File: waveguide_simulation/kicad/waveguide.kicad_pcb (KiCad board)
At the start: 2 copper layers, 5 x 5 mm, 0 parts

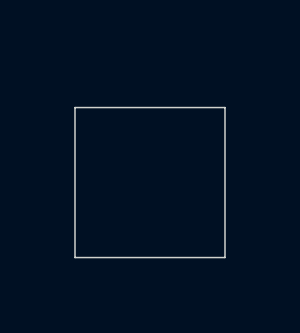
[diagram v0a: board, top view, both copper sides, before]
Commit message: [waveguide_simulation] Attempt at simulation failed, see files in relevant folder | TODO: check non-macro example (purely pcb import macro not openems macro) or check working examples first
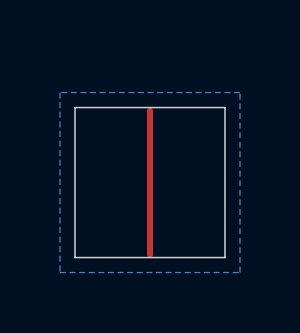
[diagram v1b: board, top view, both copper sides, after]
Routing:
- net (no net): track 0.00 -> 4.80 mm
- added copper zone on B.Cu, net (none)
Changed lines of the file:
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@@
 		(layer "Edge.Cuts")
 	)
+	(segment
+		(start 102.5 52.5)
+		(end 102.5 54.9)
+		(width 0.2)
+		(layer "F.Cu")
+		(net 0)
+	)
+	(segment
+		(start 102.5 50.1)
+		(end 102.5 52.5)
+		(width 0.2)
+		(layer "F.Cu")
+		(net 0)
+	)
+	(zone
+		(net 0)
+		(net_name "")
+		(layer "B.Cu")
+		(hatch edge 0.5)
+		(connect_pads
+			(clearance 0.5)
+		)
+		(min_thickness 0.25)
+		(filled_areas_thickness no)
+		(fill yes
+			(thermal_gap 0.5)
+			(thermal_bridge_width 0.5)
+			(island_removal_mode 1)
+			(island_area_min 10)
+		)
+		(polygon
+			(pts
+				(xy 99.5 49.5) (xy 99.5 55.5) (xy 105.5 55.5) (xy 105.5 49.5)
+			)
+		)
+	)
 )

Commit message: update waveguide and kicad project
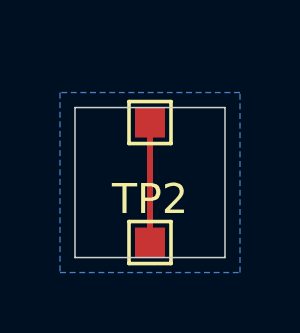
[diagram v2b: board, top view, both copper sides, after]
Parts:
- added TP1: TestPoint, TestPoint:TestPoint_Pad_1.0x1.0mm, F.Cu at (102.5, 50.5)
- added TP2: TestPoint, TestPoint:TestPoint_Pad_1.0x1.0mm, F.Cu at (102.5, 54.5)
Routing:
- net test: track 0.00 -> 4.80 mm
- net (no net): track 4.80 -> 0.00 mm

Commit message: experimented with meshing on planar waveguide
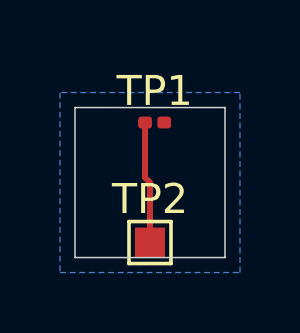
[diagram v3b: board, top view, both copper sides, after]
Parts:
- TP1: footprint TestPoint:TestPoint_Pad_1.0x1.0mm -> Resistor_SMD:R_0201_0603Metric
- moved TP1 0.16 mm to (102.7, 50.5)
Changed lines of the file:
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@@
 	(net 0 "")
 	(net 1 "test")
+	(footprint "Resistor_SMD:R_0201_0603Metric"
+		(layer "F.Cu")
+		(at 102.655 50.5)
+		(descr "Resistor SMD 0201 (0603 Metric), square (rectangular) end terminal, IPC_7351 nominal, (Body size source: https://www.vishay.com/docs/20052/crcw0201e3.pdf), generated with kicad-footprint-generator")
+		(tags "resistor")
+		(property "Reference" "TP1"
+			(at 0 -1.05 0)
+			(layer "F.SilkS")
+			(effects
+				(font
+					(size 1 1)
+					(thickness 0.15)
+				)
+			)
+		)
+		(property "Value" "TestPoint"
+			(at 0 1.05 0)
+			(layer "F.Fab")
+			(hide yes)
+			(effects
+				(font
+					(size 1 1)
+					(thickness 0.15)
+				)
+			)
+		)
+		(property "Footprint" "Resistor_SMD:R_0201_0603Metric"
+			(at 0 0 0)
+			(unlocked yes)
+			(layer "F.Fab")
+			(hide yes)
+			(effects
+				(font
+					(size 1.27 1.27)
+					(thickness 0.15)
+				)
+			)
+		)
+		(property "Datasheet" ""
+			(at 0 0 0)
+			(unlocked yes)
+			(layer "F.Fab")
+			(hide yes)
+			(effects
+				(font
+					(size 1.27 1.27)
+					(thickness 0.15)
+				)
+			)
+		)
+		(property "Description" "test point"
+			(at 0 0 0)
+			(unlocked yes)
+			(layer "F.Fab")
+			(hide yes)
+			(effects
+				(font
+					(size 1.27 1.27)
+					(thickness 0.15)
+				)
+			)
+		)
+		(property ki_fp_filters "Pin* Test*")
+		(sheetname "Root")
+		(sheetfile "waveguide.kicad_sch")
+		(attr smd)
+		(fp_line
+			(start -0.7 -0.35)
+			(end 0.7 -0.35)
+			(stroke
+				(width 0.05)
+				(type solid)
+			)
+			(layer "F.CrtYd")
+		)
+		(fp_line
+			(start -0.7 0.35)
+			(end -0.7 -0.35)
+			(stroke
+				(width 0.05)
+				(type solid)
+			)
+			(layer "F.CrtYd")
+		)
+		(fp_line
+			(start 0.7 -0.35)
+			(end 0.7 0.35)
+			(stroke
+				(width 0.05)
+				(type solid)
+			)
+			(layer "F.CrtYd")
+		)
+		(fp_line
+			(start 0.7 0.35)
+			(end -0.7 0.35)
+			(stroke
+				(width 0.05)
+				(type solid)
+			)
+			(layer "F.CrtYd")
+		)
+		(fp_line
+			(start -0.3 -0.15)
+			(end 0.3 -0.15)
+			(stroke
+				(width 0.1)
+				(type solid)
+			)
+			(layer "F.Fab")
+		)
+		(fp_line
+			(start -0.3 0.15)
+			(end -0.3 -0.15)
+			(stroke
+				(width 0.1)
+				(type solid)
+			)
+			(layer "F.Fab")
+		)
+		(fp_line
+			(start 0.3 -0.15)
+			(end 0.3 0.15)
+			(stroke
+				(width 0.1)
+				(type solid)
+			)
+			(layer "F.Fab")
+		)
+		(fp_line
+			(start 0.3 0.15)
+			(end -0.3 0.15)
+			(stroke
+				(width 0.1)
+				(type solid)
+			)
+			(layer "F.Fab")
+		)
+		(fp_text user "${REFERENCE}"
+			(at 0 -0.68 0)
+			(layer "F.Fab")
+			(effects
+				(font
+					(size 0.25 0.25)
+					(thickness 0.04)
+				)
+			)
+		)
+		(pad "" smd roundrect
+			(at -0.345 0)
+			(size 0.318 0.36)
+			(layers "F.Paste")
+			(roundrect_rratio 0.25)
+		)
+		(pad "" smd roundrect
+			(at 0.345 0)
+			(size 0.318 0.36)
+			(layers "F.Paste")
+			(roundrect_rratio 0.25)
+		)
+		(pad "1" smd roundrect
+			(at -0.32 0)
+			(size 0.46 0.4)
+			(layers "F.Cu" "F.Mask")
+			(roundrect_rratio 0.25)
+			(net 1 "test")
+			(pinfunction "1")
+			(pintype "passive")
+		)
+		(pad "2" smd roundrect
+			(at 0.32 0)
+			(size 0.46 0.4)
+			(layers "F.Cu" "F.Mask")
+			(roundrect_rratio 0.25)
+		)
+		(model "${KICAD8_3DMODEL_DIR}/Resistor_SMD.3dshapes/R_0201_0603Metric.wrl"
+			(offset
+				(xyz 0 0 0)
+			)
+			(scale
+				(xyz 1 1 1)
+			)
+			(rotate
+				(xyz 0 0 0)
+			)
+		)
+	)
 	(footprint "TestPoint:TestPoint_Pad_1.0x1.0mm"
 		(layer "F.Cu")
-		(at 102.5 50.5)
+		(at 102.5 54.5)
 		(descr "SMD rectangular pad as test Point, square 1.0mm side length")
 		(tags "test point SMD pad rectangle square")
-		(property "Reference" "TP1"
+		(property "Reference" "TP2"
 			(at 0 -1.448 0)
 			(layer "F.SilkS")
-			(hide yes)
 			(effects
 				(font
@@
 			)
 			(layer "F.CrtYd")
+		)
+		(fp_text user "${REFERENCE}"
+			(at 0 -1.45 0)
+			(layer "F.Fab")
+			(effects
+				(font
+					(size 1 1)
+					(thickness 0.15)
+				)
+			)
 		)
 		(pad "1" smd rect
@@
 		)
 	)
-	(footprint "TestPoint:TestPoint_Pad_1.0x1.0mm"
-		(layer "F.Cu")
-		(at 102.5 54.5)
-		(descr "SMD rectangular pad as test Point, square 1.0mm side length")
-		(tags "test point SMD pad rectangle square")
-		(property "Reference" "TP2"
-			(at 0 -1.448 0)
-			(layer "F.SilkS")
-			(effects
-				(font
-					(size 1 1)
-					(thickness 0.15)
-				)
-			)
-		)
-		(property "Value" "TestPoint"
-			(at 0 1.55 0)
-			(layer "F.Fab")
-			(effects
-				(font
-					(size 1 1)
-					(thickness 0.15)
-				)
-			)
-		)
-		(property "Footprint" "TestPoint:TestPoint_Pad_1.0x1.0mm"
-			(at 0 0 0)
-			(unlocked yes)
-			(layer "F.Fab")
-			(hide yes)
-			(effects
-				(font
-					(size 1.27 1.27)
-					(thickness 0.15)
-				)
-			)
-		)
-		(property "Datasheet" ""
-			(at 0 0 0)
-			(unlocked yes)
-			(layer "F.Fab")
-			(hide yes)
-			(effects
-				(font
-					(size 1.27 1.27)
-					(thickness 0.15)
-				)
-			)
-		)
-		(property "Description" "test point"
-			(at 0 0 0)
-			(unlocked yes)
-			(layer "F.Fab")
-			(hide yes)
-			(effects
-				(font
-					(size 1.27 1.27)
-					(thickness 0.15)
-				)
-			)
-		)
-		(property ki_fp_filters "Pin* Test*")
-		(sheetname "Root")
-		(sheetfile "waveguide.kicad_sch")
-		(attr exclude_from_pos_files)
-		(fp_line
-			(start -0.7 -0.7)
-			(end 0.7 -0.7)
-			(stroke
-				(width 0.12)
-				(type solid)
-			)
-			(layer "F.SilkS")
-		)
-		(fp_line
-			(start -0.7 0.7)
-			(end -0.7 -0.7)
-			(stroke
-				(width 0.12)
-				(type solid)
-			)
-			(layer "F.SilkS")
-		)
-		(fp_line
-			(start 0.7 -0.7)
-			(end 0.7 0.7)
-			(stroke
-				(width 0.12)
-				(type solid)
-			)
-			(layer "F.SilkS")
-		)
-		(fp_line
-			(start 0.7 0.7)
-			(end -0.7 0.7)
-			(stroke
-				(width 0.12)
-				(type solid)
-			)
-			(layer "F.SilkS")
-		)
-		(fp_line
-			(start -1 -1)
-			(end -1 1)
-			(stroke
-				(width 0.05)
-				(type solid)
-			)
-			(layer "F.CrtYd")
-		)
-		(fp_line
-			(start -1 -1)
-			(end 1 -1)
-			(stroke
-				(width 0.05)
-				(type solid)
-			)
-			(layer "F.CrtYd")
-		)
-		(fp_line
-			(start 1 1)
-			(end -1 1)
-			(stroke
-				(width 0.05)
-				(type solid)
-			)
-			(layer "F.CrtYd")
-		)
-		(fp_line
-			(start 1 1)
-			(end 1 -1)
-			(stroke
-				(width 0.05)
-				(type solid)
-			)
-			(layer "F.CrtYd")
-		)
-		(fp_text user "${REFERENCE}"
-			(at 0 -1.45 0)
-			(layer "F.Fab")
-			(effects
-				(font
-					(size 1 1)
-					(thickness 0.15)
-				)
-			)
-		)
-		(pad "1" smd rect
-			(at 0 0)
-			(size 1 1)
-			(layers "F.Cu" "F.Mask")
-			(net 1 "test")
-			(pinfunction "1")
-			(pintype "passive")
-		)
-	)
 	(gr_rect
 		(start 100 50)
@@
 	)
 	(segment
+		(start 102.335 52.335)
+		(end 102.5 52.5)
+		(width 0.2)
+		(layer "F.Cu")
+		(net 1)
+	)
+	(segment
+		(start 102.335 50.5)
+		(end 102.335 52.335)
+		(width 0.2)
+		(layer "F.Cu")
+		(net 1)
+	)
+	(segment
 		(start 102.5 52.5)
 		(end 102.5 54.9)
 		(width 0.2)
 		(layer "F.Cu")
-		(net 1)
-	)
-	(segment
-		(start 102.5 50.1)
-		(end 102.5 52.5)
-		(width 0.2)
-		(layer "F.Cu")
